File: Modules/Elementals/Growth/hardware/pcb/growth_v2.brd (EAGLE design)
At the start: 17.8 x 105.1 mm, 20 parts, among them J1 EURO_POWER, J2 WQP-PJ398SM6, J3 WQP-PJ398SM6, J4 WQP-PJ398SM6, J5 WQP-PJ398SM6, U1 TL072P

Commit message: Changed bypass caps to 22p for better HF response. https://northcoastsynthesis.com/news/understanding-stabilization-capacitors/
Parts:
- C5, C6: value 47p -> 22p
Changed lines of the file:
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@@
 <attribute name="VALUE" x="13.208" y="93.218" size="1.27" layer="27" ratio="10" rot="R90"/>
 </element>
-<element name="C5" library="SonicAthame" library_urn="urn:adsk.eagle:library:22327399" package="C050-024X044" package3d_urn="urn:adsk.eagle:package:26183827/3" value="47p" x="10.16" y="50.8" smashed="yes">
+<element name="C5" library="SonicAthame" library_urn="urn:adsk.eagle:library:22327399" package="C050-024X044" package3d_urn="urn:adsk.eagle:package:26183827/3" value="22p" x="10.16" y="50.8" smashed="yes">
 <attribute name="NAME" x="4.572" y="50.292" size="1.27" layer="25" ratio="10"/>
 <attribute name="POPULARITY" value="33" x="10.16" y="50.8" size="1.778" layer="27" display="off"/>
 <attribute name="SPICEPREFIX" value="C" x="10.16" y="50.8" size="1.778" layer="27" display="off"/>
 </element>
-<element name="C6" library="SonicAthame" library_urn="urn:adsk.eagle:library:22327399" package="C050-024X044" package3d_urn="urn:adsk.eagle:package:26183827/3" value="47p" x="8.89" y="38.1" smashed="yes">
+<element name="C6" library="SonicAthame" library_urn="urn:adsk.eagle:library:22327399" package="C050-024X044" package3d_urn="urn:adsk.eagle:package:26183827/3" value="22p" x="8.89" y="38.1" smashed="yes">
 <attribute name="NAME" x="7.112" y="39.497" size="1.27" layer="25" ratio="10"/>
 <attribute name="POPULARITY" value="33" x="8.89" y="38.1" size="1.778" layer="27" display="off"/>

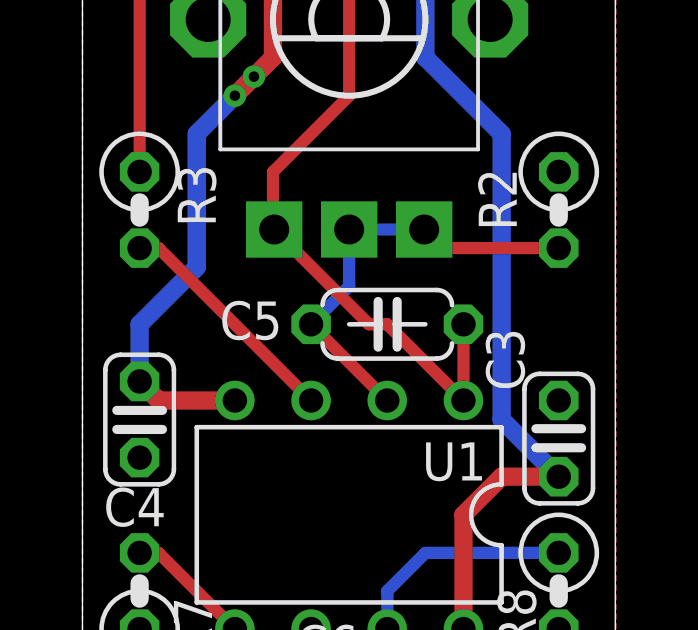
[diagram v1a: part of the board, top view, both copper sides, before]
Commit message: Minor wiring fix
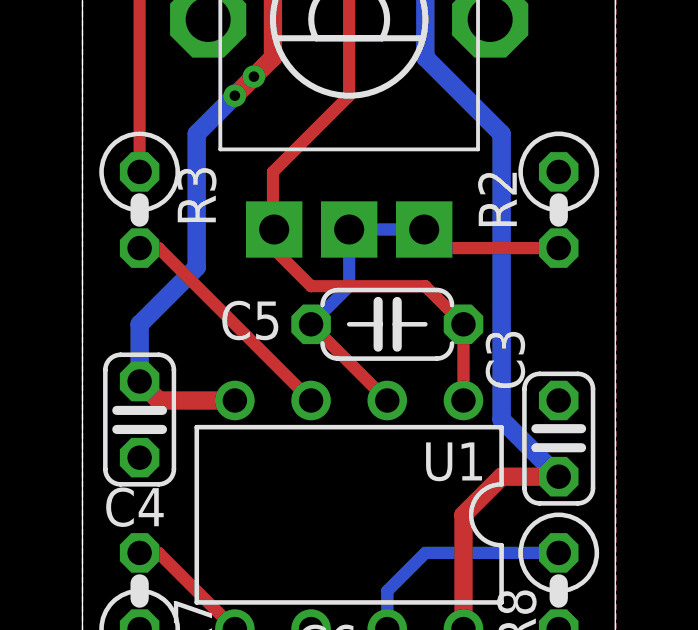
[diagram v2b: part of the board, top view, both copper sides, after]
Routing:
- net N$2: track 26.8 -> 26.1 mm
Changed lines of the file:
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@@
 <setting verticaltext="up"/>
 </settings>
-<grid distance="50" unitdist="mil" unit="mm" style="lines" multiple="1" display="yes" altdistance="25" altunitdist="mil" altunit="mil"/>
+<grid distance="50" unitdist="mil" unit="mil" style="lines" multiple="1" display="yes" altdistance="25" altunitdist="mil" altunit="mil"/>
 <layers>
 <layer number="1" name="Top" color="4" fill="1" visible="yes" active="yes"/>
@@
 <contactref element="R1" pad="P$3"/>
 <contactref element="R4" pad="1"/>
-<wire x1="12.7" y1="48.26" x2="10.16" y2="50.8" width="0.4064" layer="1"/>
-<wire x1="9.55" y1="50.8" x2="6.39" y2="53.96" width="0.4064" layer="1"/>
-<wire x1="10.16" y1="50.8" x2="9.55" y2="50.8" width="0.4064" layer="1"/>
 <wire x1="7.62" y1="67.945" x2="8.89" y2="66.675" width="0.4064" layer="1"/>
 <wire x1="8.89" y1="58.42" x2="6.35" y2="55.88" width="0.4064" layer="1"/>
@@
 <contactref element="C5" pad="2"/>
 <wire x1="12.7" y1="48.26" x2="12.7" y2="50.8" width="0.4064" layer="1"/>
+<wire x1="6.39" y1="53.96" x2="6.39" y2="53.3" width="0.4064" layer="1"/>
+<wire x1="11.43" y1="52.07" x2="12.7" y2="50.8" width="0.4064" layer="1"/>
+<wire x1="6.39" y1="53.3" x2="7.62" y2="52.07" width="0.4064" layer="1"/>
+<wire x1="7.62" y1="52.07" x2="11.43" y2="52.07" width="0.4064" layer="1"/>
 </signal>
 <signal name="N$3">

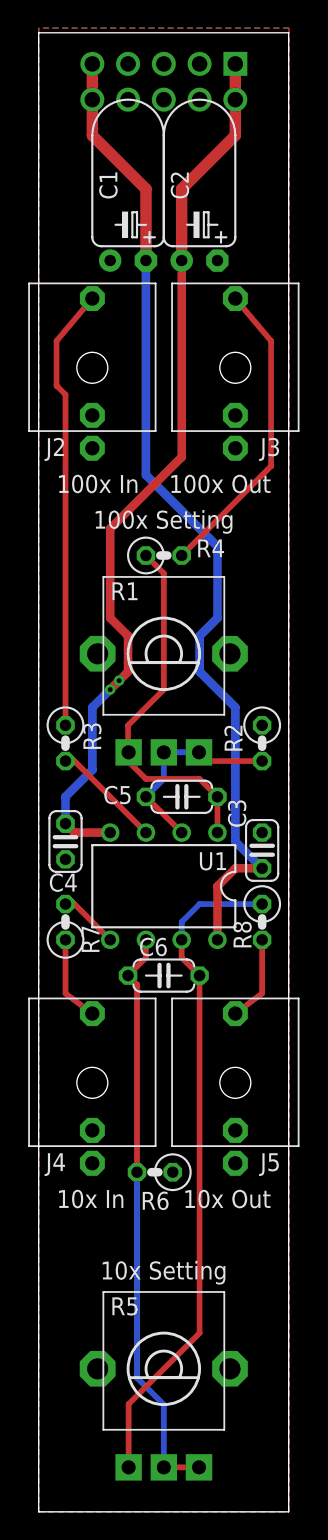
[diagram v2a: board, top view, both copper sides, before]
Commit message: Used more compact components for Elemental Growth
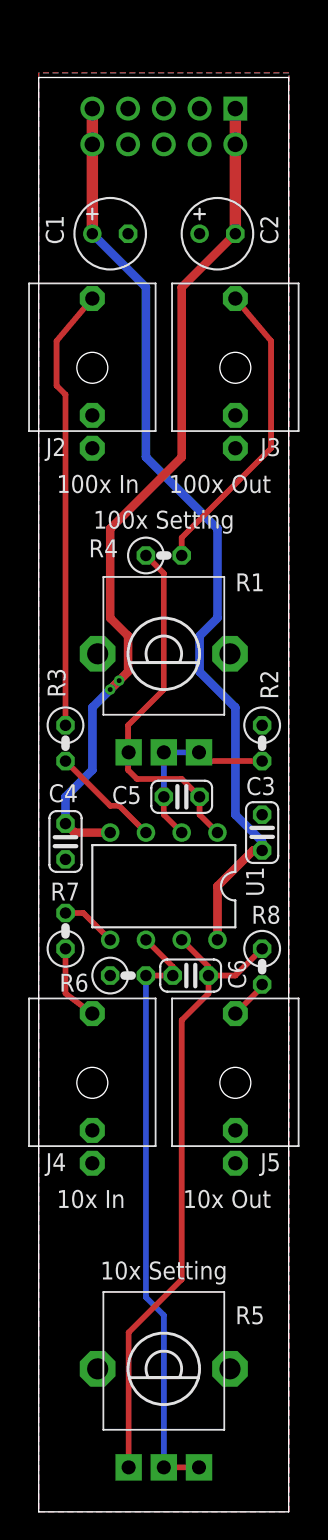
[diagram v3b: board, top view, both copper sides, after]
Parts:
- C1, C2: device SonicAthame:TT2D5L_FLIP -> SonicAthame:TT2D5
- C5, C6: device SonicAthame:C050-024X044 -> SonicAthame:C025-024X044
- moved R6 14.1 mm to (6.35, 38.1), turned to 0 degrees
- moved J1 3.17 mm to (8.89, 98.4)
- moved R8 3.17 mm to (15.9, 38.7)
- moved C1 2.29 mm to (5.08, 90.8)
- moved C2 2.29 mm to (12.7, 90.8)
- moved C6 1.90 mm to (10.8, 38.1)
- moved C3 1.27 mm to (15.9, 48.3)
- moved R7 0.63 mm to (1.91, 41.3)
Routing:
- net +12V: track 70.7 -> 66.8 mm
- net N$5: track 6.19 -> 2.85 mm
- net -12V: track 64.4 -> 61.2 mm
- net N$10: track 47.6 -> 45.2 mm
- net N$9: track 41.6 -> 43.2 mm
- net N$1: track 14.5 -> 13.5 mm
- net N$11: track 6.19 -> 5.56 mm
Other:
- board size 17.8 x 105.1 mm -> 17.8 x 101.9 mm
- board text added: "Sonic Athame is fully open-hardware and open-software! Find schematics and code on the official GitHub: github.com/nimaid/Sonic-Athame-eurorack"
- board text removed: "Sonic Athame is fully open-hardware and open-software!! Find schematics and code on the official GitHub: https://github.com/nimaid/Sonic-Athame-eurorack"
